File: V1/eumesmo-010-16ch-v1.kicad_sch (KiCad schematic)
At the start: 8 parts, among them J1 250-208, J2 250-208, J3 250-208, J4 250-208

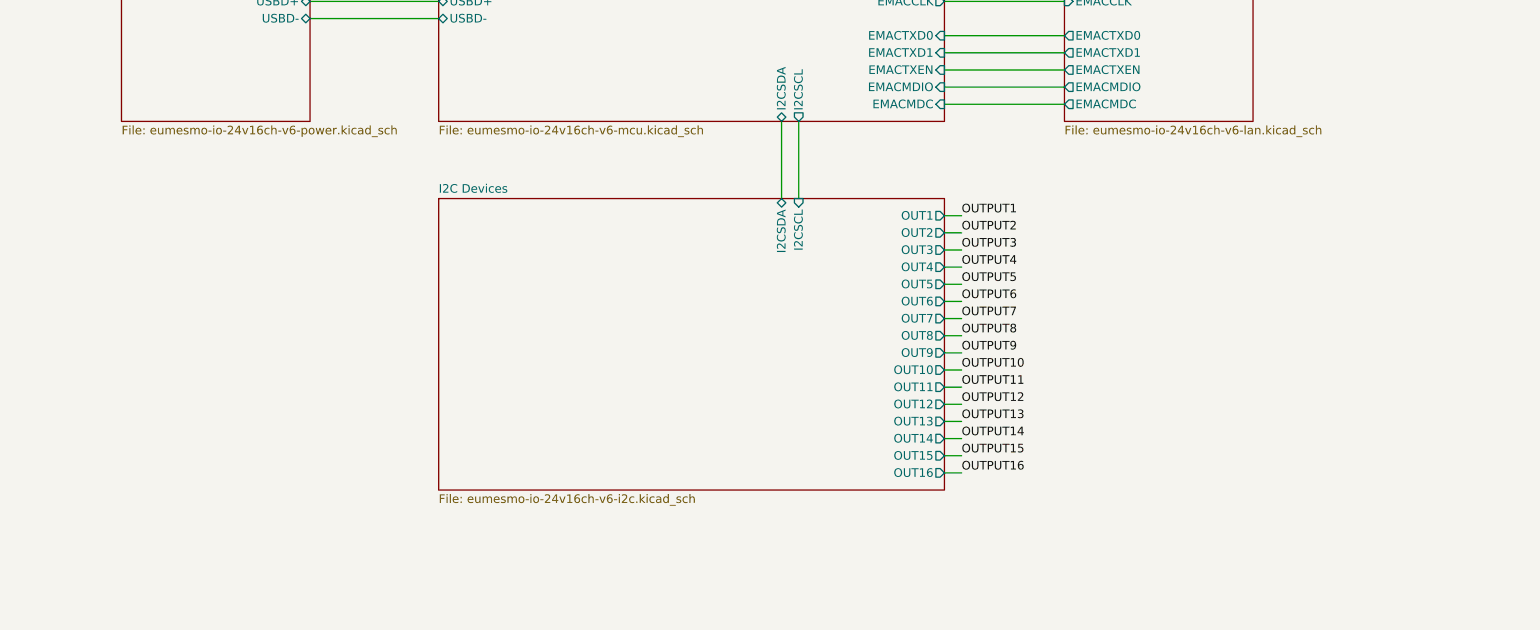
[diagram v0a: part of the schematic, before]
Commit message: Renamed all files to reflect the eumesmo branding.
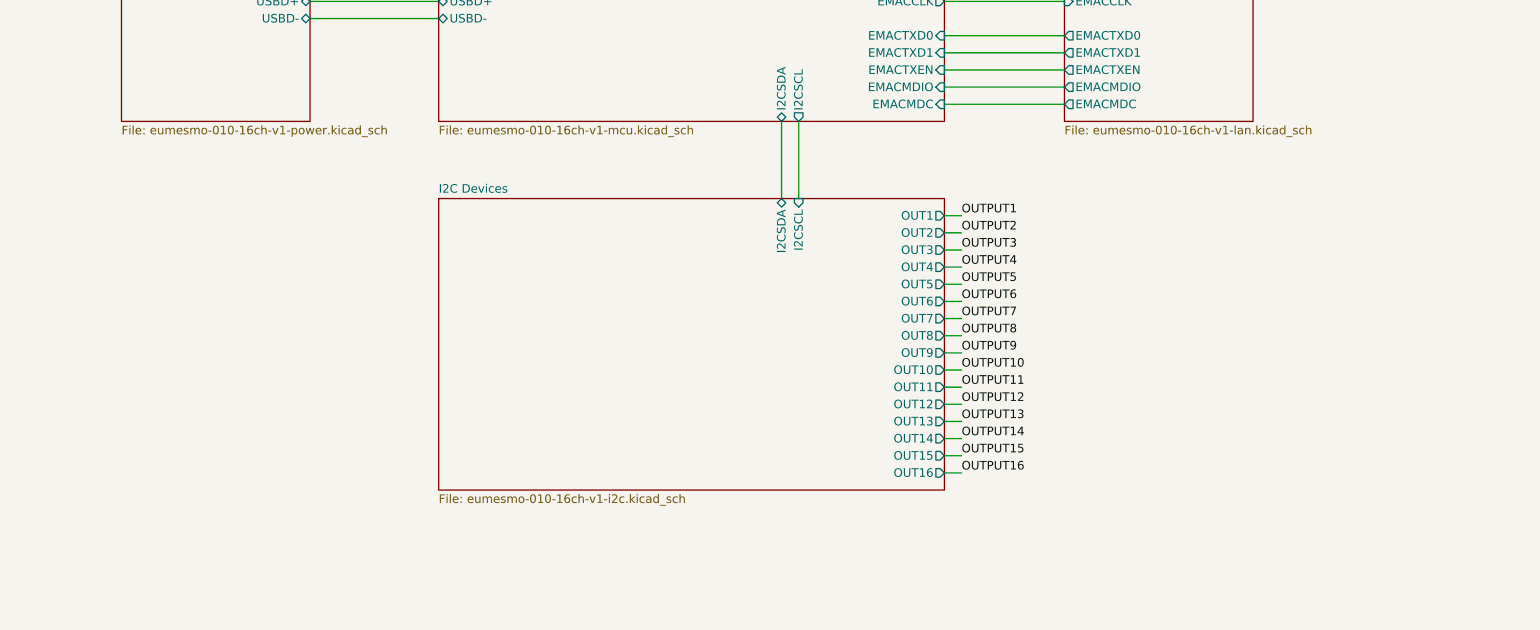
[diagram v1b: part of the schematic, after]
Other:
- sheet I2C Devices: file eumesmo-io-24v16ch-v6-i2c.kicad_sch -> eumesmo-010-16ch-v1-i2c.kicad_sch
- sheet LAN: file eumesmo-io-24v16ch-v6-lan.kicad_sch -> eumesmo-010-16ch-v1-lan.kicad_sch
- sheet MCU: file eumesmo-io-24v16ch-v6-mcu.kicad_sch -> eumesmo-010-16ch-v1-mcu.kicad_sch
- sheet Power: file eumesmo-io-24v16ch-v6-power.kicad_sch -> eumesmo-010-16ch-v1-power.kicad_sch
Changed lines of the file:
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@@
 		)
 		(instances
-			(project "eumesmo-io-24v16ch-v6"
+			(project "eumesmo-010-16ch-v1"
 				(path "/2bc5a21a-1d79-419d-a592-6852cc07b00a"
 					(reference "FID1")
@@
 		)
 		(instances
-			(project "eumesmo-io-24v16ch-v6"
+			(project "eumesmo-010-16ch-v1"
 				(path "/2bc5a21a-1d79-419d-a592-6852cc07b00a"
 					(reference "FID2")
@@
 		)
 		(instances
-			(project "eumesmo-io-24v16ch-v6"
+			(project "eumesmo-010-16ch-v1"
 				(path "/2bc5a21a-1d79-419d-a592-6852cc07b00a"
 					(reference "J4")
@@
 		)
 		(instances
-			(project "eumesmo-io-24v16ch-v6"
+			(project "eumesmo-010-16ch-v1"
 				(path "/2bc5a21a-1d79-419d-a592-6852cc07b00a"
 					(reference "J3")
@@
 		)
 		(instances
-			(project "eumesmo-io-24v16ch-v6"
+			(project "eumesmo-010-16ch-v1"
 				(path "/2bc5a21a-1d79-419d-a592-6852cc07b00a"
 					(reference "J2")
@@
 		)
 		(instances
-			(project "eumesmo-io-24v16ch-v6"
+			(project "eumesmo-010-16ch-v1"
 				(path "/2bc5a21a-1d79-419d-a592-6852cc07b00a"
 					(reference "FID4")
@@
 		)
 		(instances
-			(project "eumesmo-io-24v16ch-v6"
+			(project "eumesmo-010-16ch-v1"
 				(path "/2bc5a21a-1d79-419d-a592-6852cc07b00a"
 					(reference "FID3")
@@
 		)
 		(instances
-			(project "eumesmo-io-24v16ch-v6"
+			(project "eumesmo-010-16ch-v1"
 				(path "/2bc5a21a-1d79-419d-a592-6852cc07b00a"
 					(reference "J1")
@@
 			)
 		)
-		(property "Sheetfile" "eumesmo-io-24v16ch-v6-power.kicad_sch"
+		(property "Sheetfile" "eumesmo-010-16ch-v1-power.kicad_sch"
 			(at 118.11 60.2746 0)
 			(show_name no)
@@
 		)
 		(instances
-			(project "eumesmo-io-24v16ch-v6"
+			(project "eumesmo-010-16ch-v1"
 				(path "/2bc5a21a-1d79-419d-a592-6852cc07b00a"
 					(page "2")
@@
 			)
 		)
-		(property "Sheetfile" "eumesmo-io-24v16ch-v6-i2c.kicad_sch"
+		(property "Sheetfile" "eumesmo-010-16ch-v1-i2c.kicad_sch"
 			(at 165.1 114.8846 0)
 			(show_name no)
@@
 		)
 		(instances
-			(project "eumesmo-io-24v16ch-v6"
+			(project "eumesmo-010-16ch-v1"
 				(path "/2bc5a21a-1d79-419d-a592-6852cc07b00a"
 					(page "5")
@@
 			)
 		)
-		(property "Sheetfile" "eumesmo-io-24v16ch-v6-lan.kicad_sch"
+		(property "Sheetfile" "eumesmo-010-16ch-v1-lan.kicad_sch"
 			(at 257.81 60.2746 0)
 			(show_name no)
@@
 		)
 		(instances
-			(project "eumesmo-io-24v16ch-v6"
+			(project "eumesmo-010-16ch-v1"
 				(path "/2bc5a21a-1d79-419d-a592-6852cc07b00a"
 					(page "4")
@@
 			)
 		)
-		(property "Sheetfile" "eumesmo-io-24v16ch-v6-mcu.kicad_sch"
+		(property "Sheetfile" "eumesmo-010-16ch-v1-mcu.kicad_sch"
 			(at 165.1 60.2746 0)
 			(show_name no)
@@
 		)
 		(instances
-			(project "eumesmo-io-24v16ch-v6"
+			(project "eumesmo-010-16ch-v1"
 				(path "/2bc5a21a-1d79-419d-a592-6852cc07b00a"
 					(page "3")

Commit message: Restarting fresh
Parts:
- added J5: 250-202, Tales:TerminalBlock_Wago_250-202_1x02_P3.5mm_45Degree, symbol Connector_Generic:Conn_01x02
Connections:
- net OUT9: now reaches J4.1 (Pin_1)
- net OUT10: now reaches J4.2 (Pin_2)
- net OUT11: now reaches J4.3 (Pin_3)
- net OUT12: now reaches J4.4 (Pin_4)
- net OUT13: now reaches J4.5 (Pin_5)
- net OUT14: now reaches J4.6 (Pin_6)
- net OUT15: now reaches J4.7 (Pin_7)
- net OUT16: now reaches J4.8 (Pin_8)
- net OUT1: now reaches J3.1 (Pin_1)
- net OUT2: now reaches J3.2 (Pin_2)
- net OUT3: now reaches J3.3 (Pin_3)
- net OUT4: now reaches J3.4 (Pin_4)
- net OUT5: now reaches J3.5 (Pin_5)
- net OUT6: now reaches J3.6 (Pin_6)
- net OUT7: now reaches J3.7 (Pin_7)
- net OUT8: now reaches J3.8 (Pin_8)
- net IN9: now reaches J2.1 (Pin_1)
- net IN10: now reaches J2.2 (Pin_2)
- net IN11: now reaches J2.3 (Pin_3)
- net IN12: now reaches J2.4 (Pin_4)
- net IN13: now reaches J2.5 (Pin_5)
- net IN14: now reaches J2.6 (Pin_6)
- net IN15: now reaches J2.7 (Pin_7)
- net IN16: now reaches J2.8 (Pin_8)
- net IN1: now reaches J1.1 (Pin_1)
- net IN2: now reaches J1.2 (Pin_2)
- net IN3: now reaches J1.3 (Pin_3)
- net IN4: now reaches J1.4 (Pin_4)
- net IN5: now reaches J1.5 (Pin_5)
- net IN6: now reaches J1.6 (Pin_6)
- net IN7: now reaches J1.7 (Pin_7)
- net IN8: now reaches J1.8 (Pin_8)
- new net GNDIO: J5.1 (Pin_1), J5.2 (Pin_2)
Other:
- added sheet Input 1 (eumesmo-010-16ch-v1-inputs1-8.kicad_sch)
- added sheet Input 10 (eumesmo-010-16ch-v1-inputs9-16.kicad_sch)
- added sheet Input 11 (eumesmo-010-16ch-v1-inputs9-16.kicad_sch)
- added sheet Input 12 (eumesmo-010-16ch-v1-inputs9-16.kicad_sch)
- added sheet Input 13 (eumesmo-010-16ch-v1-inputs9-16.kicad_sch)
- added sheet Input 14 (eumesmo-010-16ch-v1-inputs9-16.kicad_sch)
- added sheet Input 15 (eumesmo-010-16ch-v1-inputs9-16.kicad_sch)
- added sheet Input 16 (eumesmo-010-16ch-v1-inputs9-16.kicad_sch)
- added sheet Input 2 (eumesmo-010-16ch-v1-inputs1-8.kicad_sch)
- added sheet Input 3 (eumesmo-010-16ch-v1-inputs1-8.kicad_sch)
- added sheet Input 4 (eumesmo-010-16ch-v1-inputs1-8.kicad_sch)
- added sheet Input 5 (eumesmo-010-16ch-v1-inputs1-8.kicad_sch)
- added sheet Input 6 (eumesmo-010-16ch-v1-inputs1-8.kicad_sch)
- added sheet Input 7 (eumesmo-010-16ch-v1-inputs1-8.kicad_sch)
- added sheet Input 8 (eumesmo-010-16ch-v1-inputs1-8.kicad_sch)
- added sheet Input 9 (eumesmo-010-16ch-v1-inputs9-16.kicad_sch)
- added sheet Output 1 (eumesmo-010-16ch-v1-outputs1-8.kicad_sch)
- added sheet Output 10 (eumesmo-010-16ch-v1-outputs9-16.kicad_sch)
- added sheet Output 11 (eumesmo-010-16ch-v1-outputs9-16.kicad_sch)
- added sheet Output 12 (eumesmo-010-16ch-v1-outputs9-16.kicad_sch)
- added sheet Output 13 (eumesmo-010-16ch-v1-outputs9-16.kicad_sch)
- added sheet Output 14 (eumesmo-010-16ch-v1-outputs9-16.kicad_sch)
- added sheet Output 15 (eumesmo-010-16ch-v1-outputs9-16.kicad_sch)
- added sheet Output 16 (eumesmo-010-16ch-v1-outputs9-16.kicad_sch)
- added sheet Output 2 (eumesmo-010-16ch-v1-outputs1-8.kicad_sch)
- added sheet Output 3 (eumesmo-010-16ch-v1-outputs1-8.kicad_sch)
- added sheet Output 4 (eumesmo-010-16ch-v1-outputs1-8.kicad_sch)
- added sheet Output 5 (eumesmo-010-16ch-v1-outputs1-8.kicad_sch)
- added sheet Output 6 (eumesmo-010-16ch-v1-outputs1-8.kicad_sch)
- added sheet Output 7 (eumesmo-010-16ch-v1-outputs1-8.kicad_sch)
- added sheet Output 8 (eumesmo-010-16ch-v1-outputs1-8.kicad_sch)
- added sheet Output 9 (eumesmo-010-16ch-v1-outputs9-16.kicad_sch)
- sheet I2C Devices ports: added 1WIREGPIO, IN1, IN10, IN11, IN12, IN13, IN14, IN15, IN16, IN2, IN3, IN4, IN5, IN6, IN7, IN8, IN9, MCPIN1INT, MCPIN2INT; removed none
- sheet MCU ports: added 1WIREGPIO, MCPIN1INT, MCPIN2INT; removed none
- note added: "GNDIO"
- note added: "INPUTS 1-8"
- note added: "INPUTS 9-16"
- note added: "OUTPUTS 1-8"
- note added: "OUTPUTS 9-16"
- note removed: "OUTPUTS 1-4"
- note removed: "OUTPUTS 13-16"
- note removed: "OUTPUTS 5-8"
- note removed: "OUTPUTS 9-12"
- moved on the sheet: J1, J2

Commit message: Development
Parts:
- removed J5: 250-202, Tales:TerminalBlock_Wago_250-202_1x02_P3.5mm_45Degree, symbol Connector_Generic:Conn_01x02
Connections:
- net IN1: no longer names the net of J1.1 (Pin_1)
- net IN10: no longer names the net of J2.2 (Pin_2)
- net IN11: no longer names the net of J2.3 (Pin_3)
- net IN12: no longer names the net of J2.4 (Pin_4)
- net IN13: no longer names the net of J2.5 (Pin_5)
- net IN14: no longer names the net of J2.6 (Pin_6)
- net IN15: no longer names the net of J2.7 (Pin_7)
- net IN16: no longer names the net of J2.8 (Pin_8)
- net IN2: no longer names the net of J1.2 (Pin_2)
- net IN3: no longer names the net of J1.3 (Pin_3)
- net IN4: no longer names the net of J1.4 (Pin_4)
- net IN5: no longer names the net of J1.5 (Pin_5)
- net IN6: no longer names the net of J1.6 (Pin_6)
- net IN7: no longer names the net of J1.7 (Pin_7)
- net IN8: no longer names the net of J1.8 (Pin_8)
- net IN9: no longer names the net of J2.1 (Pin_1)
- net OUT1: no longer names the net of J3.1 (Pin_1)
- net OUT10: no longer names the net of J4.2 (Pin_2)
- net OUT11: no longer names the net of J4.3 (Pin_3)
- net OUT12: no longer names the net of J4.4 (Pin_4)
- net OUT13: no longer names the net of J4.5 (Pin_5)
- net OUT14: no longer names the net of J4.6 (Pin_6)
- net OUT15: no longer names the net of J4.7 (Pin_7)
- net OUT16: no longer names the net of J4.8 (Pin_8)
- net OUT2: no longer names the net of J3.2 (Pin_2)
- net OUT3: no longer names the net of J3.3 (Pin_3)
- net OUT4: no longer names the net of J3.4 (Pin_4)
- net OUT5: no longer names the net of J3.5 (Pin_5)
- net OUT6: no longer names the net of J3.6 (Pin_6)
- net OUT7: no longer names the net of J3.7 (Pin_7)
- net OUT8: no longer names the net of J3.8 (Pin_8)
- net OUT9: no longer names the net of J4.1 (Pin_1)
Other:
- removed sheet Input 1
- removed sheet Input 10
- removed sheet Input 11
- removed sheet Input 12
- removed sheet Input 13
- removed sheet Input 14
- removed sheet Input 15
- removed sheet Input 16
- removed sheet Input 2
- removed sheet Input 3
- removed sheet Input 4
- removed sheet Input 5
- removed sheet Input 6
- removed sheet Input 7
- removed sheet Input 8
- removed sheet Input 9
- removed sheet Output 1
- removed sheet Output 10
- removed sheet Output 11
- removed sheet Output 12
- removed sheet Output 13
- removed sheet Output 14
- removed sheet Output 15
- removed sheet Output 16
- removed sheet Output 2
- removed sheet Output 3
- removed sheet Output 4
- removed sheet Output 5
- removed sheet Output 6
- removed sheet Output 7
- removed sheet Output 8
- removed sheet Output 9
- sheet I2C Devices ports: added none; removed 1WIREGPIO, IN1, IN10, IN11, IN12, IN13, IN14, IN15, IN16, IN2, IN3, IN4, IN5, IN6, IN7, IN8, IN9, MCPIN1INT, MCPIN2INT, OUT1, OUT10, OUT11, OUT12, OUT13, OUT14, OUT15, OUT16, OUT2, OUT3, OUT4, OUT5, OUT6, OUT7, OUT8, OUT9
- sheet MCU ports: added none; removed 1WIREGPIO, MCPIN1INT, MCPIN2INT
- note removed: "GNDIO"

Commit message: Development
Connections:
- net I2C Devices/CH13: now reaches J4.1 (Pin_1)
- net GNDA: now reaches J4.2 (Pin_2)
- net GNDA: now also J1.2 (Pin_2), J1.4 (Pin_4), J1.6 (Pin_6), J1.8 (Pin_8), J2.2 (Pin_2), J2.4 (Pin_4), J2.6 (Pin_6), J2.8 (Pin_8), J3.2 (Pin_2), J3.4 (Pin_4), J3.6 (Pin_6), J3.8 (Pin_8), J4.4 (Pin_4), J4.6 (Pin_6), J4.8 (Pin_8)
- net I2C Devices/CH14: now reaches J4.3 (Pin_3)
- net I2C Devices/CH15: now reaches J4.5 (Pin_5)
- net I2C Devices/CH16: now reaches J4.7 (Pin_7)
- net I2C Devices/CH09: now reaches J3.1 (Pin_1)
- net I2C Devices/CH10: now reaches J3.3 (Pin_3)
- net I2C Devices/CH11: now reaches J3.5 (Pin_5)
- net I2C Devices/CH12: now reaches J3.7 (Pin_7)
- net I2C Devices/CH05: now reaches J2.1 (Pin_1)
- net I2C Devices/CH06: now reaches J2.3 (Pin_3)
- net I2C Devices/CH07: now reaches J2.5 (Pin_5)
- net I2C Devices/CH08: now reaches J2.7 (Pin_7)
- net I2C Devices/CH01: now reaches J1.1 (Pin_1)
- net I2C Devices/CH02: now reaches J1.3 (Pin_3)
- net I2C Devices/CH03: now reaches J1.5 (Pin_5)
- net I2C Devices/CH04: now reaches J1.7 (Pin_7)
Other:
- sheet I2C Devices ports: added CH01, CH02, CH03, CH04, CH05, CH06, CH07, CH08, CH09, CH10, CH11, CH12, CH13, CH14, CH15, CH16; removed none
- note added: "CHANNELS 1-4"
- note added: "CHANNELS 13-16"
- note added: "CHANNELS 5-8"
- note added: "CHANNELS 9-12"
- note removed: "INPUTS 1-8"
- note removed: "INPUTS 9-16"
- note removed: "OUTPUTS 1-8"
- note removed: "OUTPUTS 9-16"
- moved on the sheet: FID1, FID2, FID3, FID4, J1, J2, J3, J4

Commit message: Development
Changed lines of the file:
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@@
 	)
 	(symbol
-		(lib_id "power:GNDA")
+		(lib_id "Tales:GNDA")
 		(at 184.15 152.4 0)
 		(unit 1)

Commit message: Development
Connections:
- net I2C Devices/CH01 renamed Analogs/CH01
- net I2C Devices/CH02 renamed Analogs/CH02
- net I2C Devices/CH03 renamed Analogs/CH03
- net I2C Devices/CH04 renamed Analogs/CH04
- net I2C Devices/CH05 renamed Analogs/CH05
- net I2C Devices/CH06 renamed Analogs/CH06
- net I2C Devices/CH07 renamed Analogs/CH07
- net I2C Devices/CH08 renamed Analogs/CH08
- net I2C Devices/CH09 renamed Analogs/CH09
- net I2C Devices/CH10 renamed Analogs/CH10
- net I2C Devices/CH11 renamed Analogs/CH11
- net I2C Devices/CH12 renamed Analogs/CH12
- net I2C Devices/CH13 renamed Analogs/CH13
- net I2C Devices/CH14 renamed Analogs/CH14
- net I2C Devices/CH15 renamed Analogs/CH15
- net I2C Devices/CH16 renamed Analogs/CH16
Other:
- added sheet Analogs (eumesmo-010-16ch-analogs.kicad_sch)
- sheet I2C Devices ports: added PWM01, PWM02, PWM03, PWM04, PWM05, PWM06, PWM07, PWM08, PWM09, PWM10, PWM11, PWM12, PWM13, PWM14, PWM15, PWM16; removed CH01, CH02, CH03, CH04, CH05, CH06, CH07, CH08, CH09, CH10, CH11, CH12, CH13, CH14, CH15, CH16
- moved on the sheet: J1, J2, J3, J4

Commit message: Development
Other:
- title: eumesmo 24V 16xIn/16xOut/1-Wire Module -> eumesmo 24V 16x 0-10V module
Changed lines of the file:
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@@
 	(paper "A4")
 	(title_block
-		(title "eumesmo 24V 16xIn/16xOut/1-Wire Module")
-		(date "2026-06-17")
-		(rev "V6.2")
+		(title "eumesmo 24V 16x 0-10V module")
+		(date "2026-06-23")
+		(rev "V1.0")
 	)
 	(text "CHANNELS 9-12"
